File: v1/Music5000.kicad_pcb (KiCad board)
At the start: 2 copper layers, 99.1 x 99.1 mm, 43 parts, among them J1 Conn_02x17_Odd_Even, J2 Conn_02x20_Odd_Even, J3 Conn_02x20_Odd_Even, J4 Conn_02x06_Top_Bottom, J5 Conn_02x06_Top_Bottom, J6 Conn_Coaxial, J7 Conn_Coaxial, J8 Conn_01x02_Male, J9 Conn_01x02_Male, Q1 2N3904, Q2 2N3904, U1 74LVC245, U2 74LVC245, U3 74LVC245, U4 IDT 71V424S12, U5 MCP4822

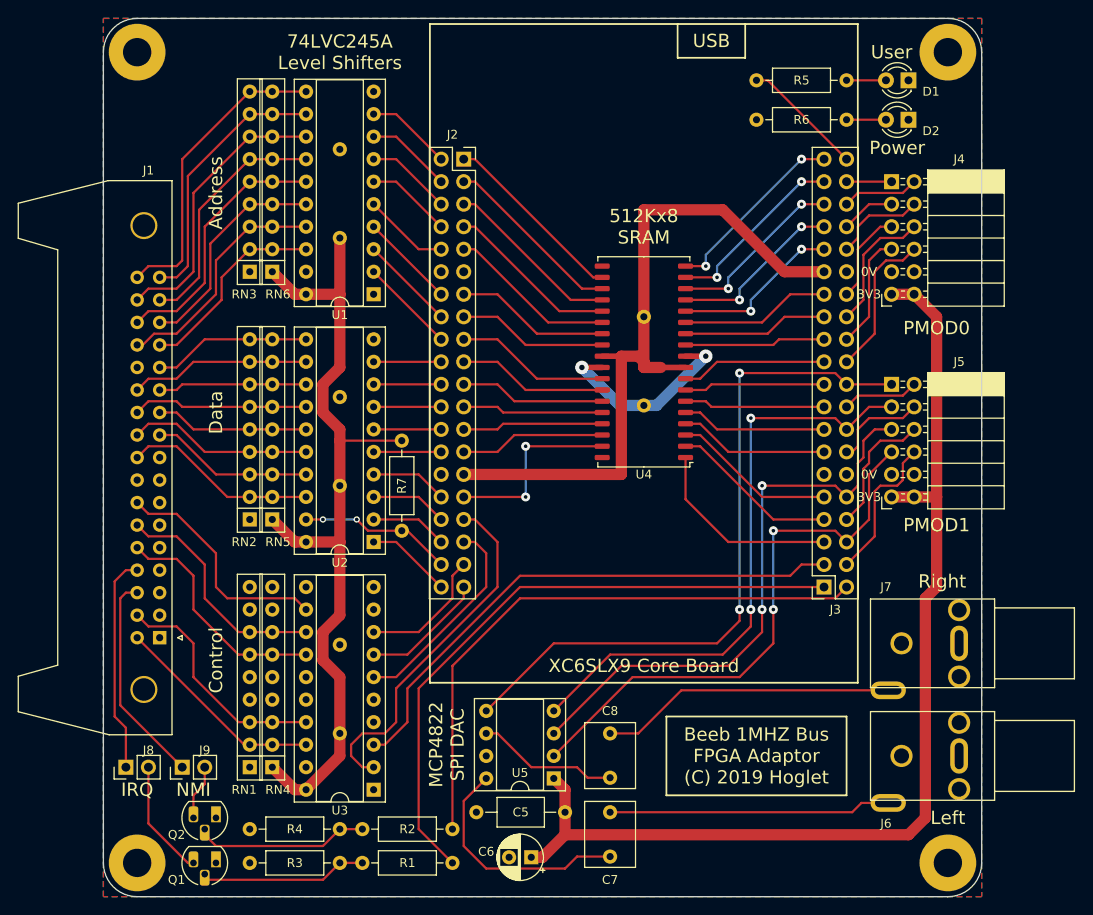
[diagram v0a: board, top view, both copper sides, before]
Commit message: PCB: Added switches
Change-Id: Ie777e91cbb6d2375a4c9e8c8aa66e1649f477c66
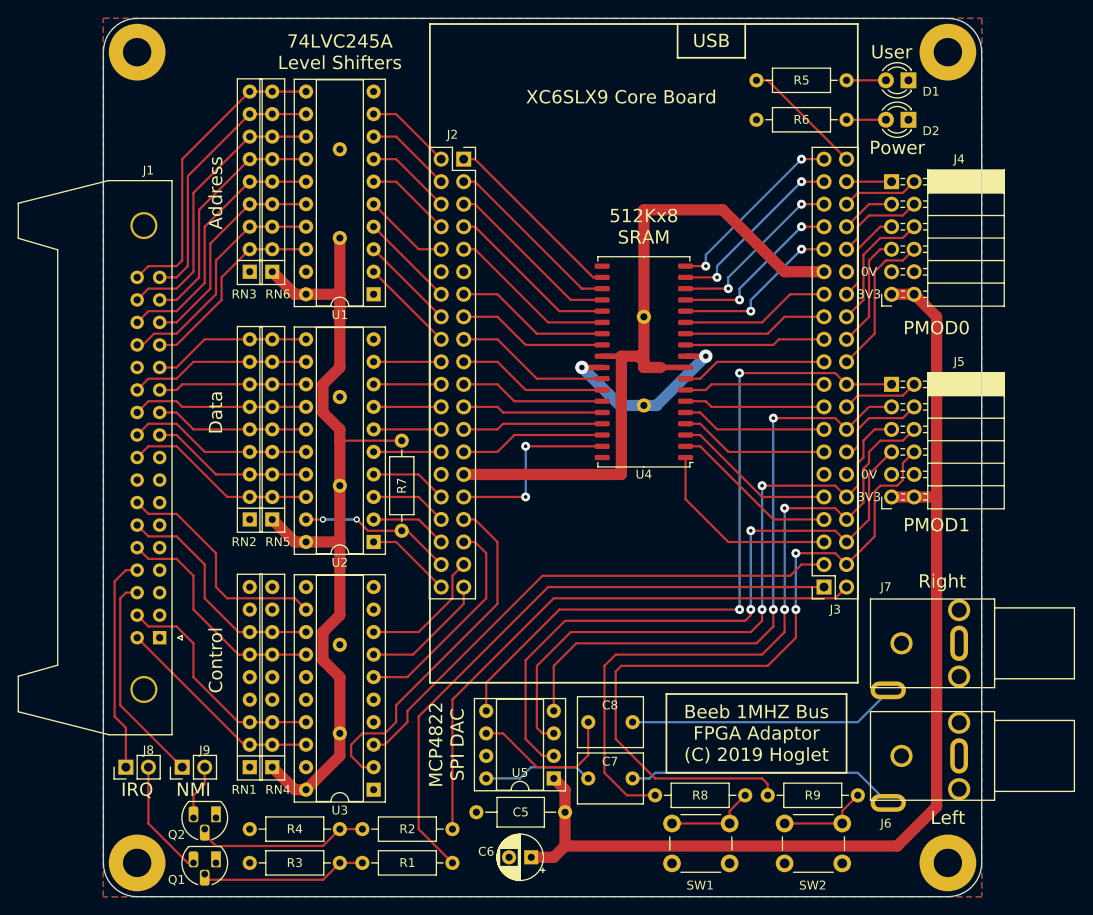
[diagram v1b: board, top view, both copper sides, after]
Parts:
- added R8: 1K0, Resistor_THT:R_Axial_DIN0207_L6.3mm_D2.5mm_P10.16mm_Horizontal, F.Cu at (112.7, 137.5)
- added R9: 1K0, Resistor_THT:R_Axial_DIN0207_L6.3mm_D2.5mm_P10.16mm_Horizontal, F.Cu at (125.4, 137.5)
- added SW1: SW_Push, Button_Switch_THT:SW_PUSH_6mm_H5mm, F.Cu at (114.6, 140.6)
- added SW2: SW_Push, Button_Switch_THT:SW_PUSH_6mm_H5mm, F.Cu at (127.3, 140.6)
- moved C7 4.58 mm to (110.2, 135.6), turned to 180 degrees
- moved C8 2.84 mm to (110.2, 129.2), turned to 180 degrees
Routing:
- net /PMOD1_7: track 17.0 -> 82.8 mm, vias 0 -> 2
- net /PMOD1_6: track 14.8 -> 77.0 mm, vias 0 -> 2
- net Net-(C7-Pad2): track 26.8 -> 12.6 mm
- net Net-(R9-Pad2): track 0.00 -> 10.4 mm
- net Net-(R8-Pad2): track 0.00 -> 10.4 mm
- net /PMOD1_3: track 63.8 -> 73.5 mm
- net /PMOD1_2: track 65.6 -> 72.8 mm
- net /PMOD1_1: track 67.1 -> 70.1 mm
- net Net-(C8-Pad1): track 33.4 -> 30.7 mm
- net /LV_NMI: track 66.5 -> 64.3 mm
- net /LV_IRQ: track 71.7 -> 69.9 mm
- net /LV_1MHZE: track 61.4 -> 60.0 mm
- net Net-(C8-Pad2): track 16.0 -> 17.5 mm
- net Net-(C7-Pad1): track 31.8 -> 30.5 mm
- net +3V3: track 300.0 -> 301.3 mm
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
